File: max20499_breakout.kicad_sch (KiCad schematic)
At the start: 1 part

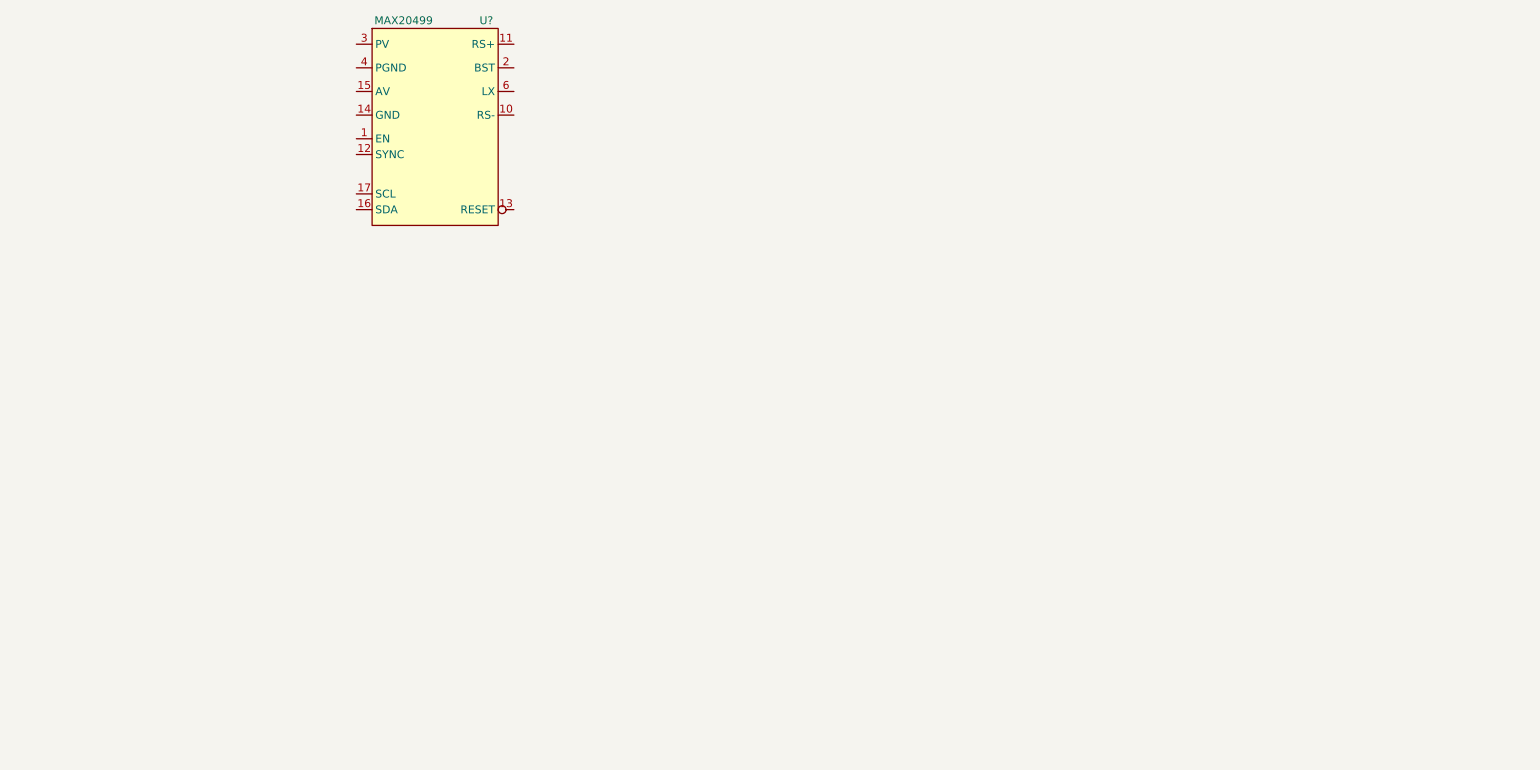
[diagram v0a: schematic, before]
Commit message: added all of the passives to schematic
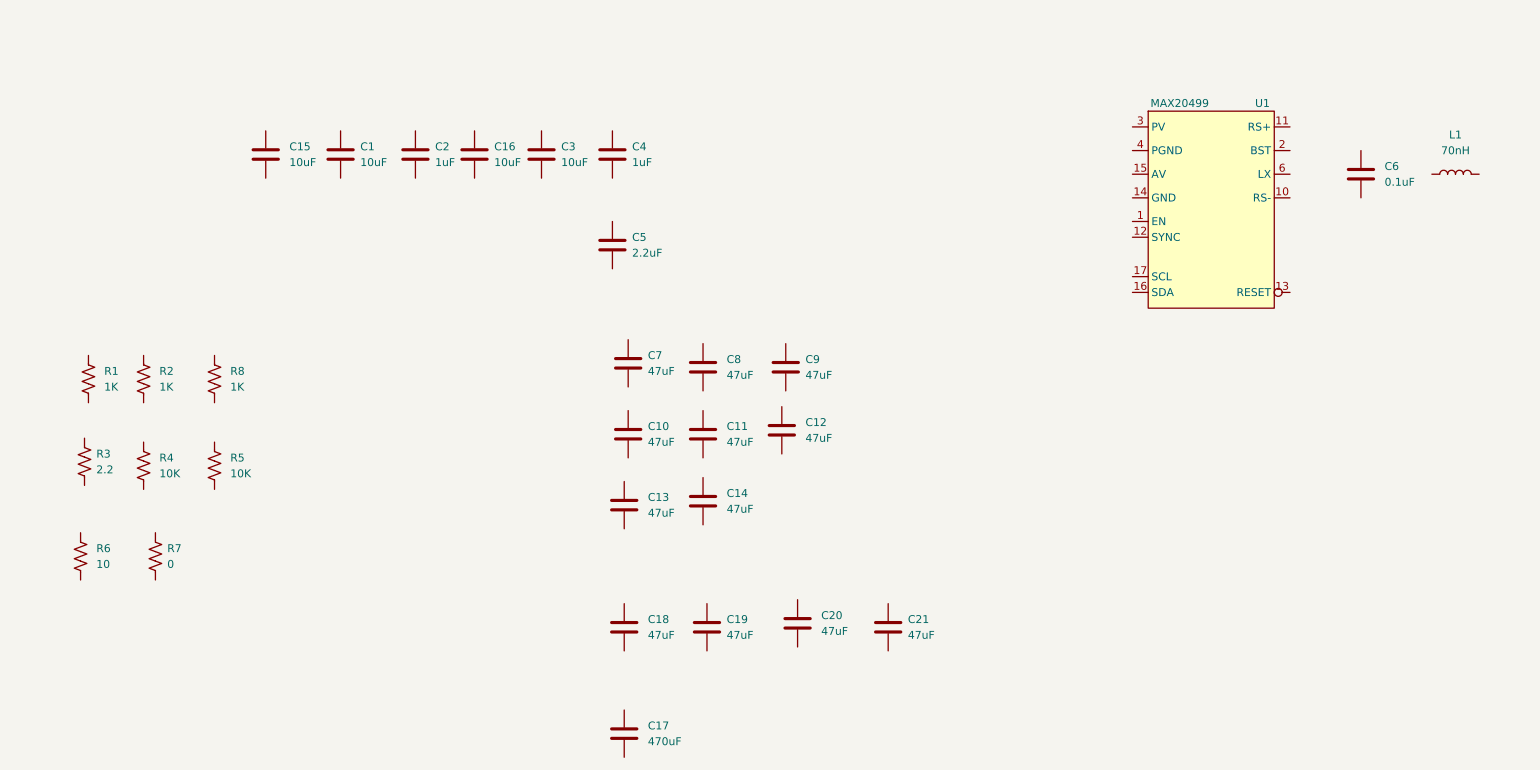
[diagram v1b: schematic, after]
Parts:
- added C1, C15, C16, C3: 10uF, Capacitor_SMD:C_0805_2012Metric, symbol Device:C
- added C10, C11, C12, C13, C14, C7, C8, C9: 47uF, Capacitor_SMD:C_1206_3216Metric, symbol Device:C
- added C17: 470uF, Capacitor_Tantalum_SMD:CP_EIA-7343-43_Kemet-X, symbol Device:C
- added C18, C19, C20, C21: 47uF, Capacitor_SMD:C_1210_3225Metric, symbol Device:C
- added C2, C4: 1uF, Capacitor_SMD:C_0603_1608Metric, symbol Device:C
- added C5: 2.2uF, Capacitor_SMD:C_0603_1608Metric, symbol Device:C
- added C6: 0.1uF, Capacitor_SMD:C_0603_1608Metric, symbol Device:C
- added L1: 70nH, symbol Device:L
- added R1, R2, R8: 1K, Resistor_SMD:R_0201_0603Metric, symbol Device:R_US
- added R3: 2.2, Resistor_SMD:R_0201_0603Metric, symbol Device:R_US
- added R4, R5: 10K, Resistor_SMD:R_0201_0603Metric, symbol Device:R_US
- added R6: 10, Resistor_SMD:R_0402_1005Metric, symbol Device:R_US
- added R7: 0, Resistor_SMD:R_0402_1005Metric, symbol Device:R_US
- gave numbers to parts that had none: 1
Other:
- moved on the sheet: U1

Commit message: finished schematic capture. started organizing PCB
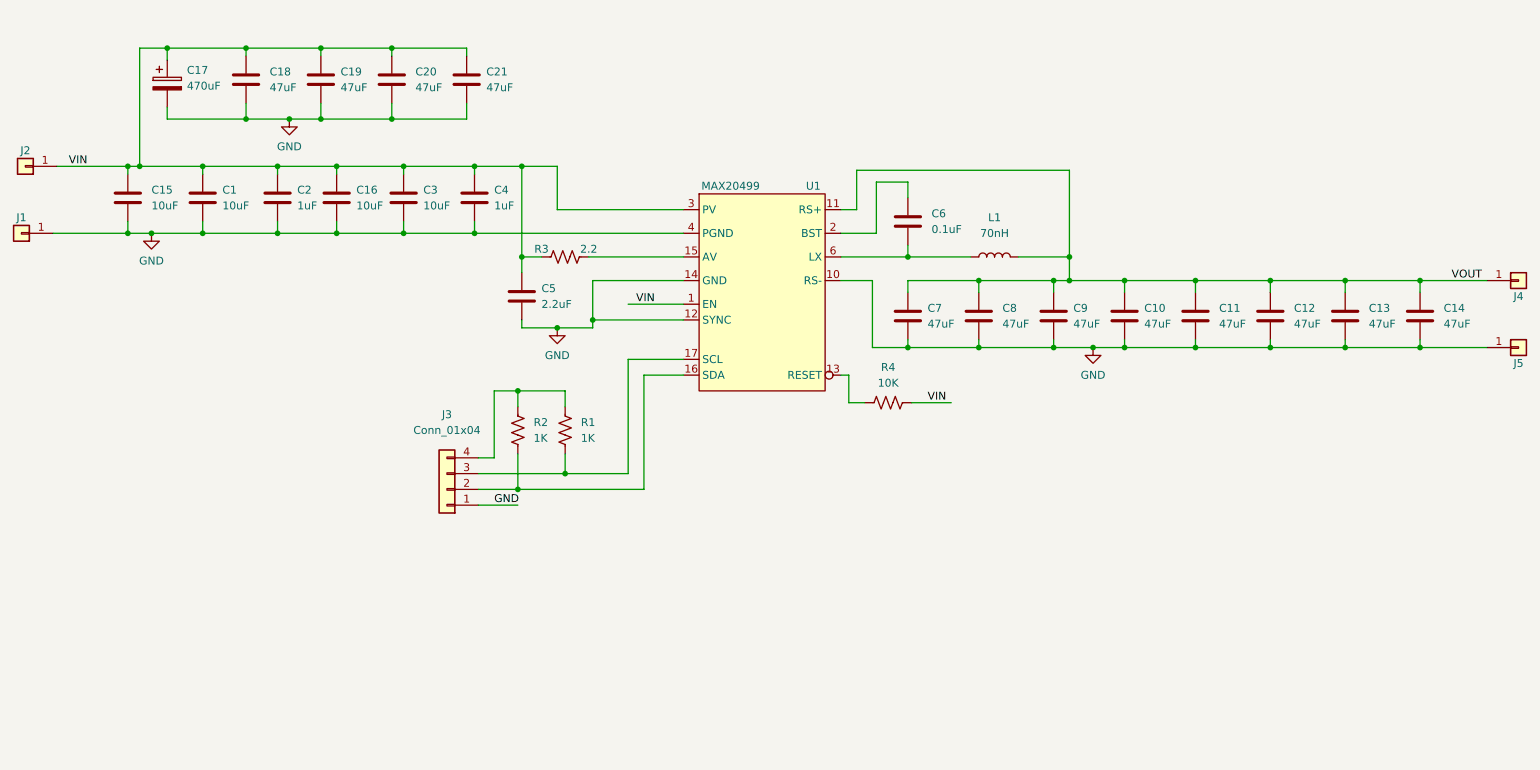
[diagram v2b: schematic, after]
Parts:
- removed C17: 470uF, Capacitor_Tantalum_SMD:CP_EIA-7343-43_Kemet-X, symbol Device:C
- removed R5: 10K, Resistor_SMD:R_0201_0603Metric, symbol Device:R_US
- removed R6: 10, Resistor_SMD:R_0402_1005Metric, symbol Device:R_US
- removed R7: 0, Resistor_SMD:R_0402_1005Metric, symbol Device:R_US
- removed R8: 1K, Resistor_SMD:R_0201_0603Metric, symbol Device:R_US
- added C17: 470uF, Capacitor_Tantalum_SMD:CP_EIA-7343-43_Kemet-X, symbol Device:C_Polarized
- added J1, J2, J4, J5: Conn_01x01, low_voltage_reg:63862-1, symbol Connector_Generic:Conn_01x01
- added J3: Conn_01x04, Connector_PinHeader_2.54mm:PinHeader_1x04_P2.54mm_Vertical, symbol Connector_Generic:Conn_01x04
- L1: footprint (none) -> low_voltage_reg:VLBU9664100LT-R07M
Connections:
- net VOUT: now reaches C9.1
- net VOUT: now also C10.1, C11.1, C12.1, C13.1, C14.1, C7.1, C8.1, L1.2, U1.11 (RS+), J4.1 (Pin_1)
- net GND: now reaches C9.2
- net GND: now also C1.2, C10.2, C11.2, C12.2, C13.2, C14.2, C15.2, C16.2, C18.2, C19.2, C2.2, C20.2, C21.2, C3.2, C4.2, C5.2, C7.2, C8.2, U1.10 (RS-), U1.12 (SYNC), U1.14 (GND), U1.4 (PGND), U1.5 (PGND), U1.7 (PGND), U1.8 (PGND), C17.2, J1.1 (Pin_1), J3.1 (Pin_1), J5.1 (Pin_1)
- net VIN: now reaches C3.1
- net VIN: now also C1.1, C15.1, C16.1, C18.1, C19.1, C2.1, C20.1, C21.1, C4.1, C5.1, R3.1, R4.1, U1.1 (EN), U1.3 (PV), U1.9 (PV), C17.1, J2.1 (Pin_1)
- net at U1.13 (RESET): now also R4.2
- net at U1.15 (AV): now also R3.2
- net at U1.16 (SDA): now also R2.2, J3.2 (Pin_2)
- net at U1.17 (SCL): now also R1.2, J3.3 (Pin_3)
- net at U1.2 (BST): now also C6.1
- net at U1.6 (LX): now also C6.2, L1.1
- net at R2.1: now also R1.1, J3.4 (Pin_4)
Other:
- title: (none) -> MAX20499 Breakout
- moved on the sheet: C1, C10, C11, C12, C13, C14, C15, C16, C18, C19, C2, C20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

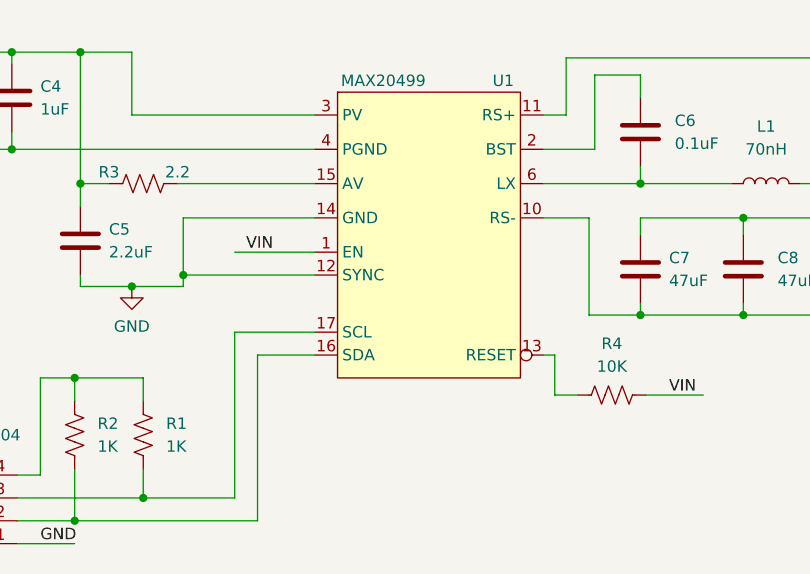
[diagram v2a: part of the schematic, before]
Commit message: routed PCB
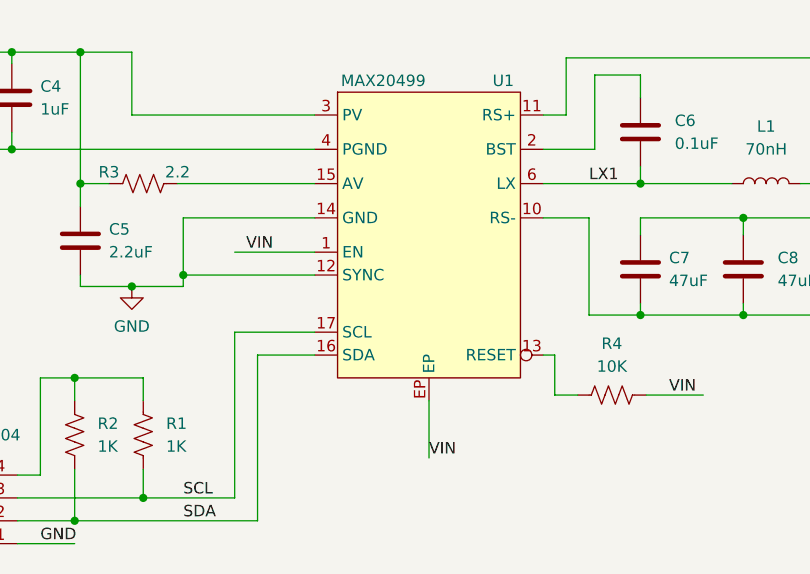
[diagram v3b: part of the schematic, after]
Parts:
- R1, R2, R3, R4: footprint Resistor_SMD:R_0201_0603Metric -> Resistor_SMD:R_0402_1005Metric
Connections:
- net VIN: now also U1.EP
- net SDA: now reaches J3.2 (Pin_2), R2.2, U1.16 (SDA)
- net SCL: now reaches J3.3 (Pin_3), R1.2, U1.17 (SCL)
- net LX1: now reaches C6.2, L1.1, U1.6 (LX)
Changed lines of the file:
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@@
+    (stroke (width 0) (type default) (color 0 0 0 0))
+  )
+  (wire (pts (xy 150.495 114.935) (xy 150.495 121.285))
     (stroke (width 0) (type default) (color 0 0 0 0))
   )
@@
   (wire (pts (xy 117.475 83.185) (xy 117.475 76.2))
     (stroke (width 0) (type default) (color 0 0 0 0))
+  )
+  (label "SCL" (at 123.19 125.73 0)
+    (effects (font (size 1.27 1.27)) (justify left bottom))
+  )
+  (label "SDA" (at 123.19 128.27 0)
+    (effects (font (size 1.27 1.27)) (justify left bottom))
+  )
+  (label "LX1" (at 168.275 90.805 0)
+    (effects (font (size 1.27 1.27)) (justify left bottom))
   )
   (label "VIN" (at 130.175 98.425 0)
@@
   )
   (label "VIN" (at 177.165 114.3 0)
+    (effects (font (size 1.27 1.27)) (justify left bottom))
+  )
+  (label "VIN" (at 150.495 121.285 0)
     (effects (font (size 1.27 1.27)) (justify left bottom))
   )
@@
     (pin "8")
     (pin "9")
+    (pin "EP")
   )
   (symbol (lib_id "Device:C") (at 111.76 97.155 0) (unit 1)
@@
     (property "Reference" "R3" (id 0) (at 114.935 89.535 90))
     (property "Value" "2.2" (id 1) (at 122.555 89.535 90))
-    (property "Footprint" "Resistor_SMD:R_0201_0603Metric" (id 2) (at 118.999 89.789 90)
+    (property "Footprint" "Resistor_SMD:R_0402_1005Metric" (id 2) (at 118.999 89.789 90)
       (effects (font (size 1.27 1.27)) hide)
     )
@@
       (effects (font (size 1.27 1.27)) (justify left))
     )
-    (property "Footprint" "Resistor_SMD:R_0201_0603Metric" (id 2) (at 112.141 118.999 90)
+    (property "Footprint" "Resistor_SMD:R_0402_1005Metric" (id 2) (at 112.141 118.999 90)
       (effects (font (size 1.27 1.27)) hide)
     )
@@
       (effects (font (size 1.27 1.27)) (justify left))
     )
-    (property "Footprint" "Resistor_SMD:R_0201_0603Metric" (id 2) (at 119.761 118.999 90)
+    (property "Footprint" "Resistor_SMD:R_0402_1005Metric" (id 2) (at 119.761 118.999 90)
       (effects (font (size 1.27 1.27)) hide)
     )
@@
     (property "Reference" "R4" (id 0) (at 170.815 108.585 90))
     (property "Value" "10K" (id 1) (at 170.815 111.125 90))
-    (property "Footprint" "Resistor_SMD:R_0201_0603Metric" (id 2) (at 170.561 115.316 90)
+    (property "Footprint" "Resistor_SMD:R_0402_1005Metric" (id 2) (at 170.561 115.316 90)
       (effects (font (size 1.27 1.27)) hide)
     )
@@
     )
     (path "/e09d5cf8-35a6-46fd-874d-dab682629338"
-      (reference "R1") (unit 1) (value "1K") (footprint "Resistor_SMD:R_0201_0603Metric")
+      (reference "R1") (unit 1) (value "1K") (footprint "Resistor_SMD:R_0402_1005Metric")
     )
     (path "/9dbbdd4b-5ac0-43d1-8a98-c5ec1fd7270b"
-      (reference "R2") (unit 1) (value "1K") (footprint "Resistor_SMD:R_0201_0603Metric")
+      (reference "R2") (unit 1) (value "1K") (footprint "Resistor_SMD:R_0402_1005Metric")
     )
     (path "/94289094-f1fa-4421-9e30-e532a5da55b3"
-      (reference "R3") (unit 1) (value "2.2") (footprint "Resistor_SMD:R_0201_0603Metric")
+      (reference "R3") (unit 1) (value "2.2") (footprint "Resistor_SMD:R_0402_1005Metric")
     )
     (path "/f1d036e1-660a-4cf8-97f1-b0019e855231"
-      (reference "R4") (unit 1) (value "10K") (footprint "Resistor_SMD:R_0201_0603Metric")
+      (reference "R4") (unit 1) (value "10K") (footprint "Resistor_SMD:R_0402_1005Metric")
     )
     (path "/35921c80-b8aa-4458-acb0-f31eb2c87e7e"

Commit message: added DK part numbers in schematic
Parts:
- C1, C15, C16, C3: DK (none) -> 1276-6685-1-ND
- C10, C11, C12, C13, C14, C7, C8, C9: DK (none) -> 1276-1167-1-ND
- C17: DK (none) -> 718-1749-1-ND
- C18, C19, C20, C21: DK (none) -> 490-10531-1-ND
- C2, C4: DK (none) -> 1276-1942-1-ND
- C5: DK (none) -> 1276-CL10Y225KP84PNCCT-ND
- C6: DK (none) -> 1276-6717-1-ND
- R1, R2: DK (none) -> 311-1.00KLRCT-ND
- R3: DK (none) -> 311-2.20LRCT-ND
- R4: DK (none) -> RMCF0402FT10K0CT-ND
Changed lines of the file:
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@@
+      (effects (font (size 1.27 1.27)) hide)
+    )
+    (property "DK" "1276-1167-1-ND" (id 4) (at 197.485 100.33 0)
       (effects (font (size 1.27 1.27)) hide)
     )
@@
       (effects (font (size 1.27 1.27)) hide)
     )
+    (property "DK" "1276-6685-1-ND" (id 4) (at 92.71 81.28 0)
+      (effects (font (size 1.27 1.27)) hide)
+    )
     (pin "1")
     (pin "2")
@@
     )
     (property "Datasheet" "~" (id 3) (at 244.475 100.33 0)
+      (effects (font (size 1.27 1.27)) hide)
+    )
+    (property "DK" "1276-1167-1-ND" (id 4) (at 244.475 100.33 0)
       (effects (font (size 1.27 1.27)) hide)
     )
@@
       (effects (font (size 1.27 1.27)) hide)
     )
+    (property "DK" "1276-CL10Y225KP84PNCCT-ND" (id 4) (at 111.76 97.155 0)
+      (effects (font (size 1.27 1.27)) hide)
+    )
     (pin "1")
     (pin "2")
@@
     )
     (property "Datasheet" "~" (id 3) (at 173.99 85.09 0)
+      (effects (font (size 1.27 1.27)) hide)
+    )
+    (property "DK" "1276-6717-1-ND" (id 4) (at 173.99 85.09 0)
       (effects (font (size 1.27 1.27)) hide)
     )
@@
       (effects (font (size 1.27 1.27)) hide)
     )
+    (property "DK" "490-10531-1-ND" (id 4) (at 102.87 62.23 0)
+      (effects (font (size 1.27 1.27)) hide)
+    )
     (pin "1")
     (pin "2")
@@
       (effects (font (size 1.27 1.27)) hide)
     )
+    (property "DK" "1276-1167-1-ND" (id 4) (at 220.345 100.33 0)
+      (effects (font (size 1.27 1.27)) hide)
+    )
     (pin "1")
     (pin "2")
@@
       (effects (font (size 1.27 1.27)) hide)
     )
+    (property "DK" "1276-1167-1-ND" (id 4) (at 256.54 100.33 0)
+      (effects (font (size 1.27 1.27)) hide)
+    )
     (pin "1")
     (pin "2")
@@
       (effects (font (size 1.27 1.27)) hide)
     )
+    (property "DK" "1276-1167-1-ND" (id 4) (at 173.99 100.33 0)
+      (effects (font (size 1.27 1.27)) hide)
+    )
     (pin "1")
     (pin "2")
@@
       (effects (font (size 1.27 1.27)) hide)
     )
+    (property "DK" "490-10531-1-ND" (id 4) (at 90.805 62.23 0)
+      (effects (font (size 1.27 1.27)) hide)
+    )
     (pin "1")
     (pin "2")
@@
     )
     (property "Datasheet" "~" (id 3) (at 54.61 62.865 0)
+      (effects (font (size 1.27 1.27)) hide)
+    )
+    (property "DK" "718-1749-1-ND" (id 4) (at 54.61 62.865 0)
       (effects (font (size 1.27 1.27)) hide)
     )
@@
       (effects (font (size 1.27 1.27)) hide)
     )
+    (property "DK" "311-2.20LRCT-ND" (id 4) (at 118.745 90.805 0)
+      (effects (font (size 1.27 1.27)) hide)
+    )
     (pin "1")
     (pin "2")
@@
       (effects (font (size 1.27 1.27)) hide)
     )
+    (property "DK" "311-1.00KLRCT-ND" (id 4) (at 111.125 118.745 0)
+      (effects (font (size 1.27 1.27)) hide)
+    )
     (pin "1")
     (pin "2")
@@
       (effects (font (size 1.27 1.27)) hide)
     )
+    (property "DK" "1276-1167-1-ND" (id 4) (at 185.42 100.33 0)
+      (effects (font (size 1.27 1.27)) hide)
+    )
     (pin "1")
     (pin "2")
@@
     )
     (property "Datasheet" "~" (id 3) (at 72.39 81.28 0)
+      (effects (font (size 1.27 1.27)) hide)
+    )
+    (property "DK" "1276-1942-1-ND" (id 4) (at 72.39 81.28 0)
       (effects (font (size 1.27 1.27)) hide)
     )
@@
       (effects (font (size 1.27 1.27)) hide)
     )
+    (property "DK" "1276-6685-1-ND" (id 4) (at 81.915 81.28 0)
+      (effects (font (size 1.27 1.27)) hide)
+    )
     (pin "1")
     (pin "2")
@@
     )
     (property "Datasheet" "~" (id 3) (at 104.14 81.28 0)
+      (effects (font (size 1.27 1.27)) hide)
+    )
+    (property "DK" "1276-1942-1-ND" (id 4) (at 104.14 81.28 0)
       (effects (font (size 1.27 1.27)) hide)
     )
@@
       (effects (font (size 1.27 1.27)) hide)
     )
+    (property "DK" "490-10531-1-ND" (id 4) (at 67.31 62.23 0)
+      (effects (font (size 1.27 1.27)) hide)
+    )
     (pin "1")
     (pin "2")
@@
       (effects (font (size 1.27 1.27)) hide)
     )
+    (property "DK" "1276-6685-1-ND" (id 4) (at 48.26 81.28 0)
+      (effects (font (size 1.27 1.27)) hide)
+    )
     (pin "1")
     (pin "2")
@@
       (effects (font (size 1.27 1.27)) hide)
     )
+    (property "DK" "490-10531-1-ND" (id 4) (at 79.375 62.23 0)
+      (effects (font (size 1.27 1.27)) hide)
+    )
     (pin "1")
     (pin "2")
@@
       (effects (font (size 1.27 1.27)) hide)
     )
+    (property "DK" "1276-1167-1-ND" (id 4) (at 232.41 100.33 0)
+      (effects (font (size 1.27 1.27)) hide)
+    )
     (pin "1")
     (pin "2")
@@
       (effects (font (size 1.27 1.27)) hide)
     )
+    (property "DK" "1276-1167-1-ND" (id 4) (at 208.915 100.33 0)
+      (effects (font (size 1.27 1.27)) hide)
+    )
     (pin "1")
     (pin "2")
@@
       (effects (font (size 1.27 1.27)) hide)
     )
+    (property "DK" "311-1.00KLRCT-ND" (id 4) (at 118.745 118.745 0)
+      (effects (font (size 1.27 1.27)) hide)
+    )
     (pin "1")
     (pin "2")
@@
     )
     (property "Datasheet" "~" (id 3) (at 60.325 81.28 0)
+      (effects (font (size 1.27 1.27)) hide)
+    )
+    (property "DK" "1276-6685-1-ND" (id 4) (at 60.325 81.28 0)
       (effects (font (size 1.27 1.27)) hide)
     )
@@
       (effects (font (size 1.27 1.27)) hide)
     )
+    (property "DK" "RMCF0402FT10K0CT-ND" (id 4) (at 170.815 114.3 0)
+      (effects (font (size 1.27 1.27)) hide)
+    )
